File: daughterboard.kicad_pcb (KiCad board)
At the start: 4 copper layers, 70 x 90 mm, 61 parts, among them J1 USB_OTG, J10 J, J11 J, J12 J, J13 J, J14 J, J15 J, J16 J, J17 J, J2 MotorA, J24 J, J25 J, J26 J, J27 J, J28 J, J29 J, J3 MotorB, J30 J, J31 J, J32 J, J33 QTR-8A, J34 J, J35 J, J4 BARREL_JACK, J5 Debug, J6 J, J7 J, J8 J, J9 J, SW1 Reset, U1 LD1117S33CTR, U2 TB6612FNG, U3 EFM32G230F128, Y1 Crystal

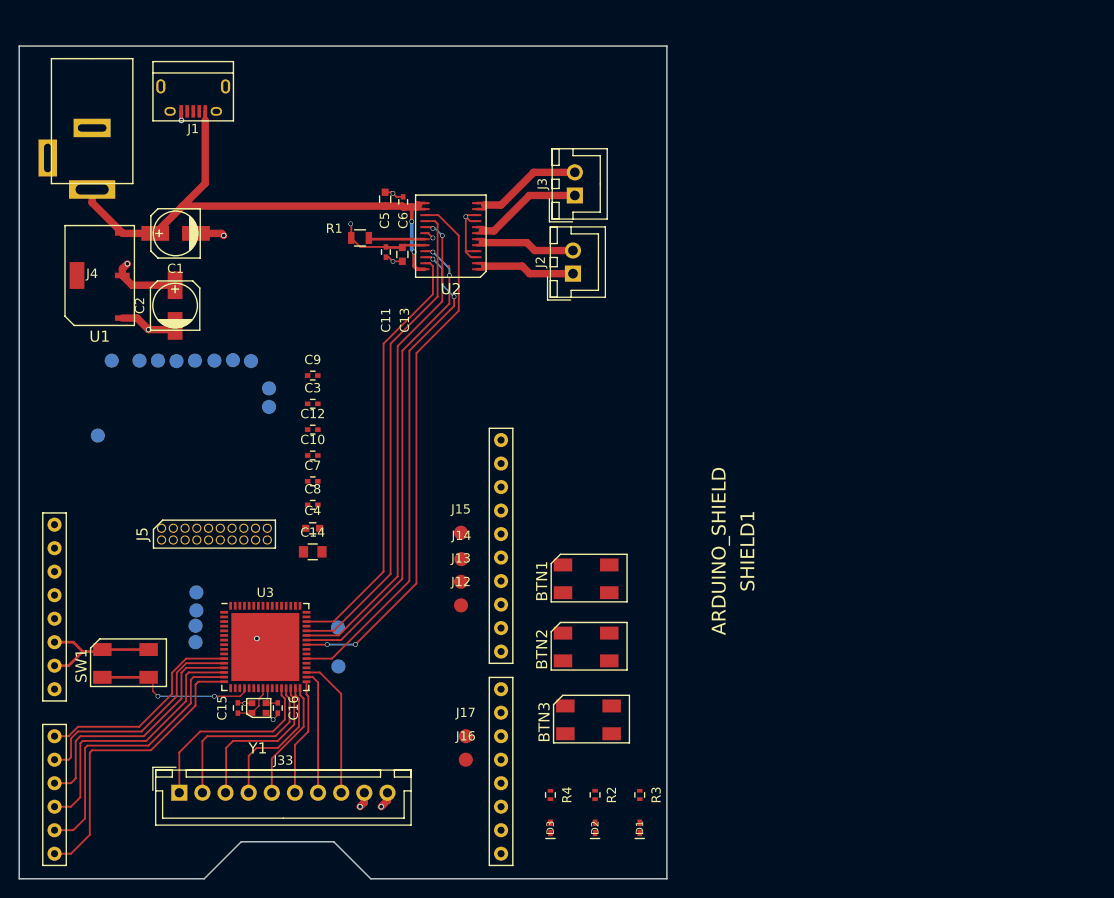
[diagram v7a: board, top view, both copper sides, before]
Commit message: Add routing of pads etc
Nearly finished, just _one_ capacitor remaining
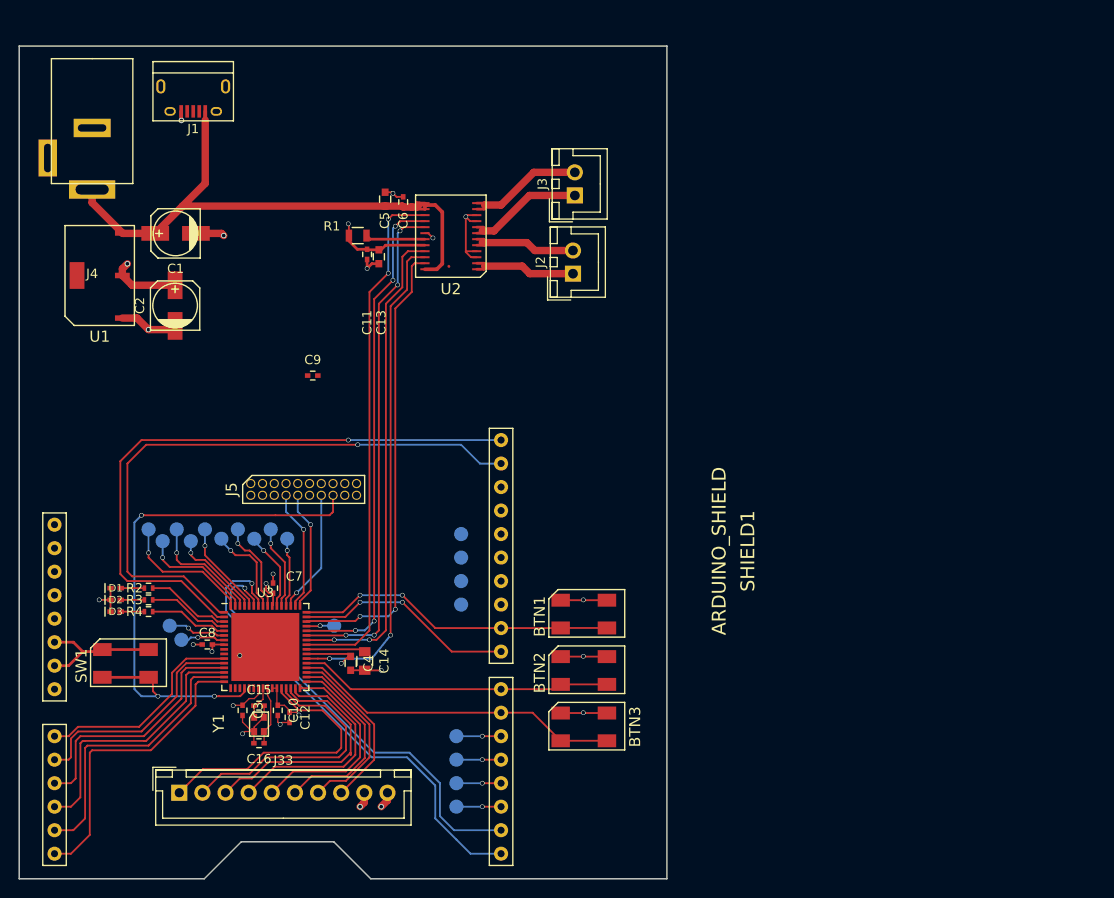
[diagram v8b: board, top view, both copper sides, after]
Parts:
- removed J8, J9: J, Measurement_Points:Measurement_Point_Round-SMD-Pad_Small
- J12, J13, J14, J15, J16, J17: moved to B.Cu
- moved D1 62.3 mm to (74.4, 116.6), turned to 0 degrees
- moved D2 57.4 mm to (74.4, 117.9), turned to 0 degrees
- moved R3 57.1 mm to (78.0, 117.9), turned to 180 degrees
- moved R2 53.2 mm to (78.0, 116.6), turned to 180 degrees
- moved D3 52.5 mm to (74.4, 119.1), turned to 0 degrees
- moved R4 47.7 mm to (78.0, 119.1), turned to 180 degrees
- moved J10 35.2 mm to (111.3, 140.2)
- moved J11 34.9 mm to (111.3, 137.7)
- moved C3 34.0 mm to (88.1, 129.8), turned to 270 degrees
- moved C12 31.2 mm to (93.2, 130.6), turned to 270 degrees
- moved C10 27.8 mm to (91.9, 129.8), turned to 270 degrees
- moved J27 19.8 mm to (82.5, 111.5)
- moved J32 19.7 mm to (89.4, 111.3)
- moved J29 19.7 mm to (79.5, 111.5)
- moved J30 19.6 mm to (93.0, 111.3)
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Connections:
- BTN1 pad 3: /EFM32/PA15 -> /EFM32/PC15
- BTN1 pad 4: /EFM32/PA15 -> /EFM32/PC15
- BTN2 pad 3: /EFM32/PA10 -> /EFM32/PC6
- BTN2 pad 4: /EFM32/PA10 -> /EFM32/PC6
- BTN3 pad 3: /EFM32/PA9 -> /EFM32/PD8
- BTN3 pad 4: /EFM32/PA9 -> /EFM32/PD8
- J7 pad 1: /EFM32/PC14 -> /EFM32/PA15
- SHIELD1 pad 6: /EFM32/PC1 -> /EFM32/PD8
- SHIELD1 pad 7: /EFM32/PC0 -> /EFM32/PC6
- SHIELD1 pad 8: /EFM32/PC6 -> /EFM32/PC14
- SHIELD1 pad 9: Net-(SHIELD1-Pad9) -> /EFM32/PC15
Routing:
- net /EFM32/SCL: track 0.00 -> 67.4 mm, vias 0 -> 1
- net /EFM32/SDA: track 0.00 -> 66.0 mm, vias 0 -> 1
- net /EFM32/TX: track 0.00 -> 51.1 mm, vias 0 -> 1
- net /EFM32/RX: track 0.00 -> 47.4 mm, vias 0 -> 1
- net /EFM32/RESETn: track 17.0 -> 61.6 mm, vias 2 -> 3
- net +3V3: track 20.2 -> 56.8 mm, vias 3 -> 11
- net /EFM32/PD8: track 0.00 -> 35.7 mm
- net /EFM32/PC15: track 0.00 -> 34.7 mm, vias 0 -> 2
- net /EFM32/PC6: track 0.00 -> 33.8 mm
- net /EFM32/PC14: track 0.00 -> 23.9 mm, vias 0 -> 2
- net GND: track 74.1 -> 92.3 mm, vias 11 -> 15
- net /EFM32/PA15: track 0.00 -> 14.5 mm, vias 0 -> 1
- net /EFM32/PF2: track 0.00 -> 13.3 mm, vias 0 -> 1
- net /EFM32/PF1: track 0.00 -> 13.1 mm, vias 0 -> 1
- net /EFM32/PF0: track 0.00 -> 13.0 mm, vias 0 -> 1
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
